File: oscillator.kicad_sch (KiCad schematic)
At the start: 3 parts, among them Y1 SG-210STF 24.5760ML0

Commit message: redoing file add
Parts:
- renumbered C21 to C25, R38 to R34
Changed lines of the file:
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@@
 		(dnp no)
 		(fields_autoplaced yes)
-		(property "Reference" "C21"
+		(property "Reference" "C25"
 			(at 145.8341 81.3441 0)
 			(effects
@@
 			(project ""
 				(path "/afe1fbe1-30b6-4eb7-94cf-5d2700d51271/30c88bb8-75d7-4f91-9e19-1fd8d6337b61"
-					(reference "C21")
+					(reference "C25")
 					(unit 1)
 				)
@@
 		(dnp no)
 		(fields_autoplaced yes)
-		(property "Reference" "#PWR049"
+		(property "Reference" "#PWR053"
 			(at 138.43 111.76 0)
 			(effects
@@
 			(project "pcm3168a_euro1"
 				(path "/afe1fbe1-30b6-4eb7-94cf-5d2700d51271/30c88bb8-75d7-4f91-9e19-1fd8d6337b61"
-					(reference "#PWR049")
+					(reference "#PWR053")
 					(unit 1)
 				)
@@
 		(dnp no)
 		(fields_autoplaced yes)
-		(property "Reference" "#PWR048"
+		(property "Reference" "#PWR052"
 			(at 138.43 81.28 0)
 			(effects
@@
 			(project ""
 				(path "/afe1fbe1-30b6-4eb7-94cf-5d2700d51271/30c88bb8-75d7-4f91-9e19-1fd8d6337b61"
-					(reference "#PWR048")
+					(reference "#PWR052")
 					(unit 1)
 				)
@@
 		(dnp no)
 		(fields_autoplaced yes)
-		(property "Reference" "#PWR050"
+		(property "Reference" "#PWR054"
 			(at 143.51 91.44 0)
 			(effects
@@
 			(project "pcm3168a_euro1"
 				(path "/afe1fbe1-30b6-4eb7-94cf-5d2700d51271/30c88bb8-75d7-4f91-9e19-1fd8d6337b61"
-					(reference "#PWR050")
+					(reference "#PWR054")
 					(unit 1)
 				)
@@
 		(on_board yes)
 		(dnp no)
-		(property "Reference" "R38"
+		(property "Reference" "R34"
 			(at 123.19 92.71 90)
 			(effects
@@
 			(project "pcm3168a_euro1"
 				(path "/afe1fbe1-30b6-4eb7-94cf-5d2700d51271/30c88bb8-75d7-4f91-9e19-1fd8d6337b61"
-					(reference "R38")
-					(unit 1)
-				)
+					(reference "R34")
+					(unit 1)
+				)

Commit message: commiting before making large changes. simplifying design, hard tying jumpers for more well defined operation modes. removing slave/slave capability, removing i2c
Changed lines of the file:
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@@
 				(font
 					(size 1.27 1.27)
+					(thickness 0.1588)
 				)
 			)

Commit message: WIP layout
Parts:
- added C26: C_Small, Capacitor_SMD:C_0603_1608Metric, symbol Device:C_Small
- added C27: 100nF, Capacitor_SMD:C_0603_1608Metric, symbol Device:C
- added C94: 4.7uF, Capacitor_SMD:C_0603_1608Metric, symbol Device:C_Small
- added J13: Conn_Coaxial, Connector_Coaxial:SMA_Amphenol_901-144_Vertical, symbol Connector:Conn_Coaxial
- added R35: 0, Resistor_SMD:R_0603_1608Metric, symbol Device:R_Small
- added R36: R_Small, Resistor_SMD:R_0603_1608Metric, symbol Device:R_Small
- added R37, R38: 22, Resistor_SMD:R_0603_1608Metric, symbol Device:R_Small
- added SW1: SW_Push, symbol Switch:SW_Push
- added U6: 74LVC1G17, Package_TO_SOT_SMD:SOT-23-5, symbol 74xGxx:74LVC1G17
- R34: value 0 -> 22k; now not fitted
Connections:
- net GND: now also C26.2, C27.2, C94.2, J13.2 (Ext), R36.1, SW1.1, U6.3 (GND)
- net VDD: now also C27.1, U6.5 (VCC)
- net at R34.2, Y1.1 (~{ST}): now also C94.1, SW1.2
- net OSC_OUT: no longer names the net of Y1.3 (OUT)
- net OSC_OUT: now also R38.1
- new net: J13.1 (In), R37.2
- new net: R37.1, U6.4
- new net: R35.1, R38.2
- new net: C26.1, R35.2, R36.2, U6.2
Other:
- moved on the sheet: C25, Y1

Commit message: WIP layout
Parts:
- removed SW1: SW_Push, symbol Switch:SW_Push
- added J16: Conn_01x02_Pin, Connector_PinHeader_2.54mm:PinHeader_1x02_P2.54mm_Vertical, symbol Connector:Conn_01x02_Pin
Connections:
- net GND: now also J16.2 (Pin_2)
- net at C94.1, R34.2, Y1.1 (~{ST}): now also J16.1 (Pin_1)
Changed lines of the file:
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@@
 	(wire
 		(pts
-			(xy 66.04 132.08) (xy 66.04 133.35)
+			(xy 78.74 130.81) (xy 78.74 133.35)
 		)
 		(stroke
@@
 	(wire
 		(pts
-			(xy 78.74 130.81) (xy 78.74 133.35)
+			(xy 160.02 110.49) (xy 160.02 115.57)
 		)
 		(stroke
@@
 	(wire
 		(pts
-			(xy 160.02 110.49) (xy 160.02 115.57)
+			(xy 66.04 121.92) (xy 66.04 110.49)
 		)
 		(stroke
@@
 	(wire
 		(pts
-			(xy 66.04 121.92) (xy 66.04 110.49)
+			(xy 91.44 90.17) (xy 91.44 91.44)
 		)
 		(stroke
@@
 	(wire
 		(pts
-			(xy 91.44 90.17) (xy 91.44 91.44)
+			(xy 66.04 110.49) (xy 78.74 110.49)
 		)
 		(stroke
@@
 	(wire
 		(pts
-			(xy 66.04 110.49) (xy 78.74 110.49)
+			(xy 99.06 110.49) (xy 102.87 110.49)
 		)
 		(stroke
@@
 	(wire
 		(pts
-			(xy 99.06 110.49) (xy 102.87 110.49)
+			(xy 66.04 124.46) (xy 66.04 133.35)
 		)
 		(stroke
@@
 	)
 	(symbol
-		(lib_id "Switch:SW_Push")
-		(at 66.04 127 90)
-		(unit 1)
-		(exclude_from_sim no)
-		(in_bom yes)
-		(on_board yes)
-		(dnp no)
-		(fields_autoplaced yes)
-		(property "Reference" "SW1"
-			(at 67.183 125.7878 90)
-			(effects
-				(font
-					(size 1.27 1.27)
-				)
-				(justify right)
-			)
-		)
-		(property "Value" "SW_Push"
-			(at 67.183 128.2121 90)
-			(effects
-				(font
-					(size 1.27 1.27)
-				)
-				(justify right)
-			)
-		)
-		(property "Footprint" ""
-			(at 60.96 127 0)
-			(effects
-				(font
-					(size 1.27 1.27)
-				)
-				(hide yes)
-			)
-		)
-		(property "Datasheet" "~"
-			(at 60.96 127 0)
-			(effects
-				(font
-					(size 1.27 1.27)
-				)
-				(hide yes)
-			)
-		)
-		(property "Description" "Push button switch, generic, two pins"
-			(at 66.04 127 0)
-			(effects
-				(font
-					(size 1.27 1.27)
-				)
-				(hide yes)
-			)
-		)
-		(pin "1"
-		)
-		(pin "2"
-		)
-		(instances
-			(project ""
-				(path "/afe1fbe1-30b6-4eb7-94cf-5d2700d51271/30c88bb8-75d7-4f91-9e19-1fd8d6337b61"
-					(reference "SW1")
-					(unit 1)
-				)
-			)
-		)
-	)
-	(symbol
 		(lib_id "power:GND")
 		(at 219.71 115.57 0)
@@
 					(unit 1)
 				)
+			)
+		)
+	)
+	(symbol
+		(lib_id "Connector:Conn_01x02_Pin")
+		(at 60.96 121.92 0)
+		(unit 1)
+		(exclude_from_sim no)
+		(in_bom yes)
+		(on_board yes)
+		(dnp no)
+		(fields_autoplaced yes)
+		(property "Reference" "J16"
+			(at 61.595 117.6993 0)
+			(effects
+				(font
+					(size 1.27 1.27)
+				)
+			)
+		)
+		(property "Value" "Conn_01x02_Pin"
+			(at 61.595 120.1236 0)
+			(effects
+				(font
+					(size 1.27 1.27)
+				)
+			)
+		)
+		(property "Footprint" "Connector_PinHeader_2.54mm:PinHeader_1x02_P2.54mm_Vertical"
+			(at 60.96 121.92 0)
+			(effects
+				(font
+					(size 1.27 1.27)
+				)
+				(hide yes)
+			)
+		)
+		(property "Datasheet" "~"
+			(at 60.96 121.92 0)
+			(effects
+				(font
+					(size 1.27 1.27)
+				)
+				(hide yes)
+			)
+		)
+		(property "Description" "Generic connector, single row, 01x02, script generated"
+			(at 60.96 121.92 0)
+			(effects
+				(font
+					(size 1.27 1.27)
+				)
+				(hide yes)
+			)
+		)
+		(pin "2"
+		)
+		(pin "1"
+		)
+		(instances
+			(project "pcm3168a_euro1"
+				(path "/afe1fbe1-30b6-4eb7-94cf-5d2700d51271/30c88bb8-75d7-4f91-9e19-1fd8d6337b61"
+					(reference "J16")
+					(unit 1)
+				)

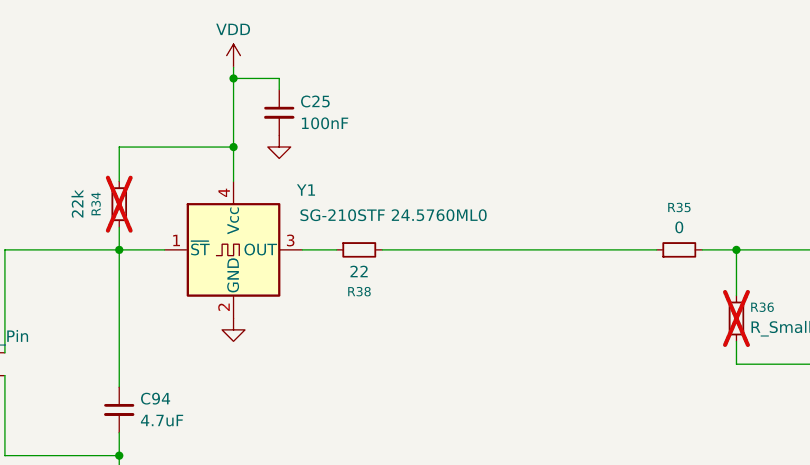
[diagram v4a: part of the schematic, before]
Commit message: WIP need to fix OPA1637 footprint
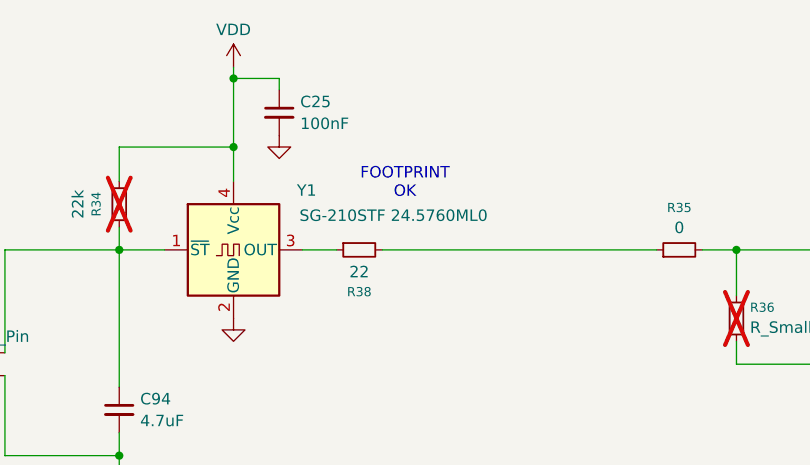
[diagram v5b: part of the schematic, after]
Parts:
- J13: footprint Connector_Coaxial:SMA_Amphenol_901-144_Vertical -> pcm3168a_euro1:SMA_Amphenol_901-144_Vertical_awl1
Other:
- note added: "FOOTPRINT OK"
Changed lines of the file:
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@@
 	(generator_version "9.0")
 	(paper "A4")
+	(text "FOOTPRINT\nOK"
+		(exclude_from_sim no)
+		(at 110.49 103.124 0)
+		(effects
+			(font
+				(size 1.27 1.27)
+				(color 255 0 15 1)
+			)
+		)
+	)
 	(junction
 		(at 78.74 133.35)
@@
 			)
 		)
-		(property "Footprint" "Connector_Coaxial:SMA_Amphenol_901-144_Vertical"
+		(property "Footprint" "pcm3168a_euro1:SMA_Amphenol_901-144_Vertical_awl1"
 			(at 219.71 110.49 0)
 			(effects

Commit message: added part numbers
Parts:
- C25, C27: PN (none) -> GCJ188R71H104KA12D
- C94: PN (none) -> GRM188Z71A475ME15D
- J16: PN (none) -> 61300211121
- R34: value 22k -> 4.7k; PN (none) -> ERA-3AEB472V; now fitted
- R35: PN (none) -> CRCW06030000Z0EA
- R37, R38: PN (none) -> CRCW060322R0FKEAC
- U6: PN (none) -> SN74LVC1G17DBVR
- Y1: PN (none) -> SG-210STF 24.5760ML0
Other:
- note removed: "FOOTPRINT OK"
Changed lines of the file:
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@@
 	(generator_version "9.0")
 	(paper "A4")
-	(text "FOOTPRINT\nOK"
-		(exclude_from_sim no)
-		(at 110.49 103.124 0)
-		(effects
-			(font
-				(size 1.27 1.27)
-				(color 255 0 15 1)
-			)
-		)
-	)
 	(junction
 		(at 78.74 133.35)
@@
 			)
 		)
+		(property "PN" "GCJ188R71H104KA12D"
+			(at 96.52 95.25 0)
+			(effects
+				(font
+					(size 1.27 1.27)
+				)
+				(hide yes)
+			)
+		)
 		(pin "2"
 		)
@@
 			)
 		)
+		(property "PN" "GCJ188R71H104KA12D"
+			(at 185.42 96.52 0)
+			(effects
+				(font
+					(size 1.27 1.27)
+				)
+				(hide yes)
+			)
+		)
 		(pin "1"
 		)
@@
 			)
 		)
+		(property "PN" "CRCW060322R0FKEAC"
+			(at 203.2 110.49 90)
+			(effects
+				(font
+					(size 1.27 1.27)
+				)
+				(hide yes)
+			)
+		)
 		(pin "2"
 		)
@@
 		(property "Description" "Resistor, small symbol"
 			(at 105.41 110.49 0)
+			(effects
+				(font
+					(size 1.27 1.27)
+				)
+				(hide yes)
+			)
+		)
+		(property "PN" "CRCW060322R0FKEAC"
+			(at 105.41 110.49 90)
 			(effects
 				(font
@@
 			)
 		)
+		(property "PN" "SG-210STF 24.5760ML0"
+			(at 91.44 110.49 0)
+			(effects
+				(font
+					(size 1.27 1.27)
+				)
+				(hide yes)
+			)
+		)
 		(pin "2"
 		)
@@
 			)
 		)
+		(property "PN" "GRM188Z71A475ME15D"
+			(at 78.74 128.27 0)
+			(effects
+				(font
+					(size 1.27 1.27)
+				)
+				(hide yes)
+			)
+		)
 		(pin "2"
 		)
@@
 			)
 		)
+		(property "PN" "CRCW06030000Z0EA"
+			(at 140.97 110.49 90)
+			(effects
+				(font
+					(size 1.27 1.27)
+				)
+				(hide yes)
+			)
+		)
 		(pin "2"
 		)
@@
 			)
 		)
+		(property "PN" "SN74LVC1G17DBVR"
+			(at 184.15 110.49 0)
+			(effects
+				(font
+					(size 1.27 1.27)
+				)
+				(hide yes)
+			)
+		)
 		(pin "2"
 		)
@@
 			)
 		)
+		(property "PN" "61300211121"
+			(at 60.96 121.92 0)
+			(effects
+				(font
+					(size 1.27 1.27)
+				)
+				(hide yes)
+			)
+		)
 		(pin "2"
 		)
@@
 		(in_bom yes)
 		(on_board yes)
-		(dnp yes)
+		(dnp no)
 		(property "Reference" "R34"
 			(at 76.2 105.41 90)
@@
 			)
 		)
-		(property "Value" "22k"
+		(property "Value" "4.7k"
 			(at 74.168 105.41 90)
 			(effects
@@
 			(effects
 				(font
+					(size 1.27 1.27)
+				)
+				(hide yes)
+			)
+		)
+		(property "PN" "ERA-3AEB472V"
+			(at 78.74 105.41 90)
+			(effects
+				(font
